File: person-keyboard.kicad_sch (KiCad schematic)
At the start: 36 parts, among them J1 USB_C_Receptacle_USB2.0_16P, SW106 SW_Push, SW107 SW_Push, U1 RP2040, U2 AMS1117-3.3, U3 W25Q128JVS, U4 PRTR5V0U2X, Y1 ABM8-272-T3

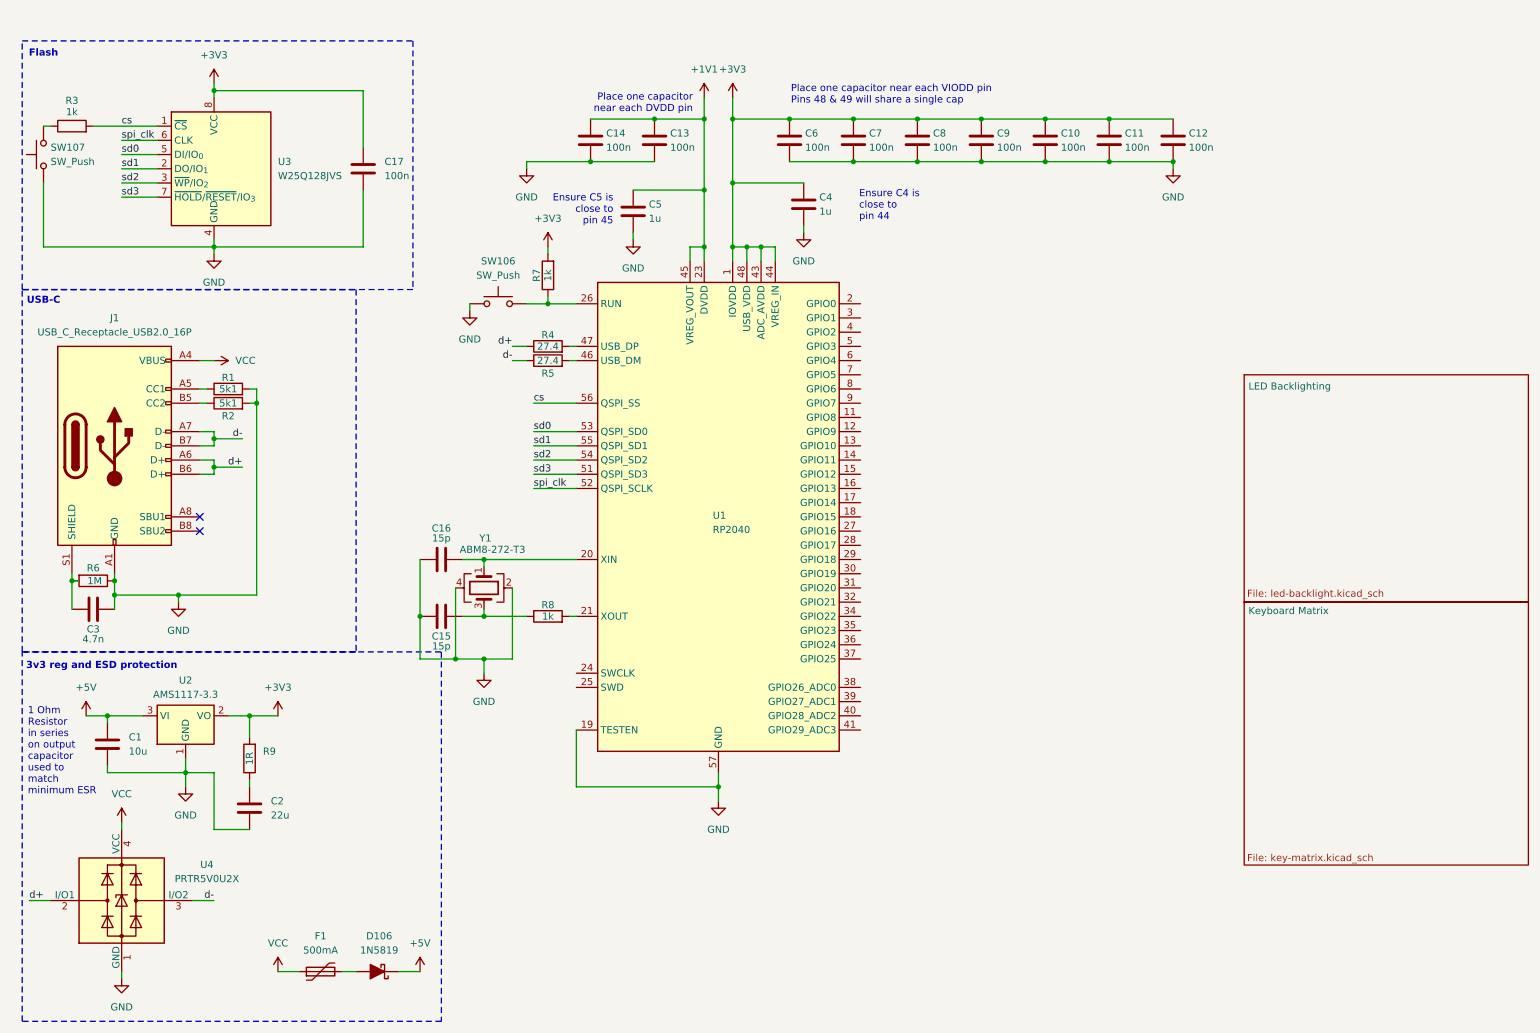
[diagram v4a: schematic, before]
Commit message: Started keyboard matrix, completed all rows, completed numpad columns
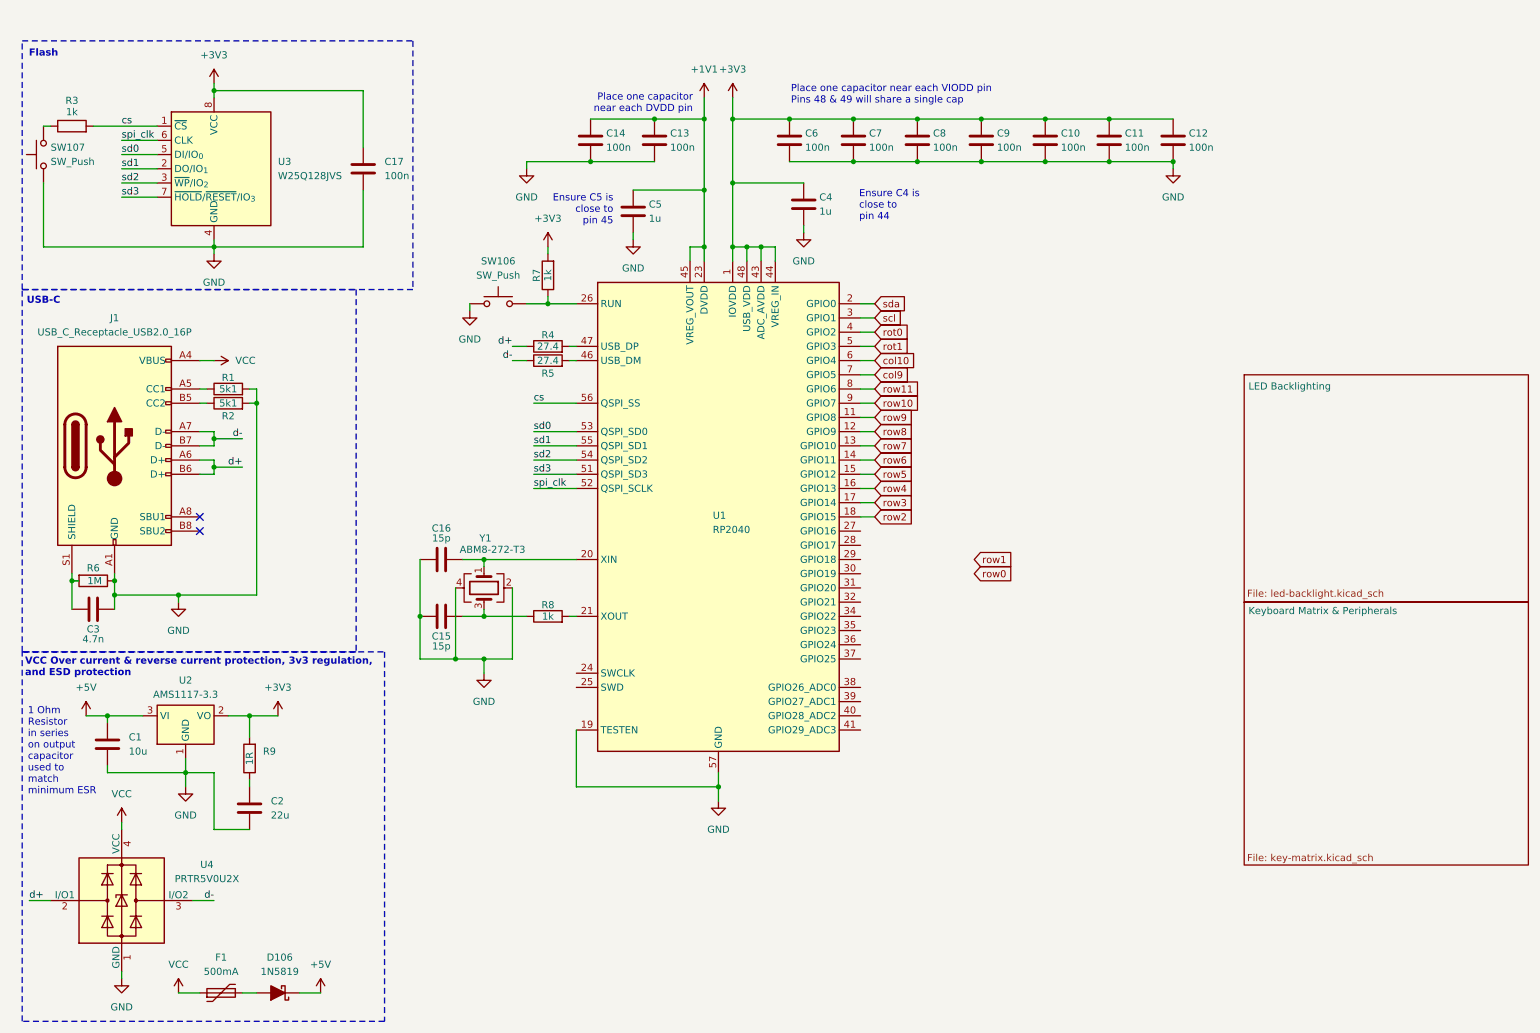
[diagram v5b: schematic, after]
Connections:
- net row9: now reaches U1.11 (GPIO8)
- net row8: now reaches U1.12 (GPIO9)
- net row7: now reaches U1.13 (GPIO10)
- net row6: now reaches U1.14 (GPIO11)
- net row5: now reaches U1.15 (GPIO12)
- net row4: now reaches U1.16 (GPIO13)
- net row3: now reaches U1.17 (GPIO14)
- net row2: now reaches U1.18 (GPIO15)
- net sda: now reaches U1.2 (GPIO0)
- net scl: now reaches U1.3 (GPIO1)
- net rot0: now reaches U1.4 (GPIO2)
- net rot1: now reaches U1.5 (GPIO3)
- net col10: now reaches U1.6 (GPIO4)
- net col9: now reaches U1.7 (GPIO5)
- net row11: now reaches U1.8 (GPIO6)
- net row10: now reaches U1.9 (GPIO7)
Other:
- sheet Keyboard Matrix renamed Keyboard Matrix & Peripherals
- note added: "VCC Over current & reverse current protection, 3v3 regulation, and ESD protection"
- note removed: "3v3 reg and ESD protection"
- moved on the sheet: D106, F1

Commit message: Started Main matrix
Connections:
- net row0: now also U1.28 (GPIO17)
- net row1: now also U1.27 (GPIO16)
- net col8: now reaches U1.29 (GPIO18)
- net col7: now reaches U1.30 (GPIO19)
- net col6: now reaches U1.31 (GPIO20)
- net col5: now reaches U1.32 (GPIO21)
- net col4: now reaches U1.34 (GPIO22)
- net col3: now reaches U1.35 (GPIO23)
- net col2: now reaches U1.36 (GPIO24)
- net col1: now reaches U1.37 (GPIO25)
- net col0: now reaches U1.38 (GPIO26_ADC0)
